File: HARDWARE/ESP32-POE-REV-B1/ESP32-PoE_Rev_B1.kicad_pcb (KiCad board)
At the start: 2 copper layers, 28 x 75 mm, 123 parts, among them Q1 Q12MHz/20pF/10ppm/4P/3.2x2.5mm, Q2 BC817-40(SOT23), Q3 BC817-40(SOT23), T1 DTC114YKA(SOT-23), U1 CH340T(SSOP20W), U3 MCP73833(MSOP10), U4 LAN8710A-EZC(QFN32), U7 SY8089AAAC(SOT23-5), U8 Si3402-B-GM(QFN-20_5x5mm), U9 ESP-WROOM-32

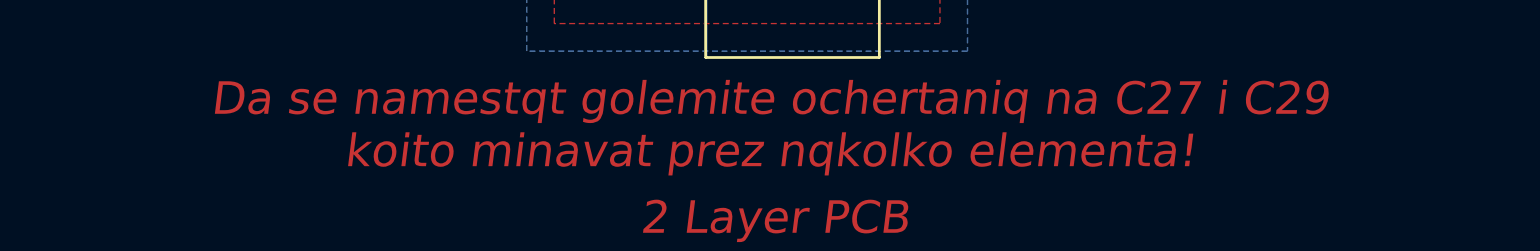
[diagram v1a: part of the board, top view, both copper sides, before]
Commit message: Update
Removed redundant text
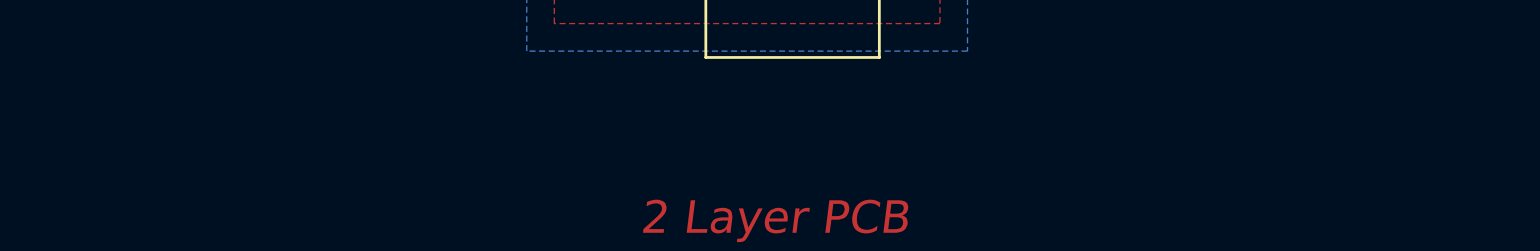
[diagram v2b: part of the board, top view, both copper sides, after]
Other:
- board text removed: "Da se namestqt golemite ochertaniq na C27 i C29 koito minavat prez nqkolko elementa!"
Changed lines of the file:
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@@
-(kicad_pcb (version 20171130) (host pcbnew 6.0.0-rc1-unknown-f85b147~66~ubuntu16.04.1)
+(kicad_pcb (version 20171130) (host pcbnew 6.0.0-rc1-unknown-80b25aa~66~ubuntu16.04.1)
   (general
     (thickness 1.6)
-    (drawings 24)
+    (drawings 23)
     (tracks 2605)
     (zones 0)
@@
     (35 F.Paste user hide)
     (36 B.SilkS user)
-    (37 F.SilkS user hide)
+    (37 F.SilkS user)
     (38 B.Mask user hide)
     (39 F.Mask user hide)
@@
     (effects (font (size 1.016 1.016) (thickness 0.254)))
   )
-  (gr_text "Da se namestqt golemite ochertaniq na C27 i C29 \nkoito minavat prez nqkolko elementa!" (at 106.2482 182.0672) (layer F.Cu)
-    (effects (font (size 3 3) (thickness 0.5) italic))
-  )
   (gr_text 1 (at 108.839 108.585) (layer B.SilkS)
     (effects (font (size 0.762 0.762) (thickness 0.1905)) (justify mirror))
@@
   (segment (start 111.125 127.762) (end 112.014 127.762) (width 0.4064) (layer B.Cu) (net 45))
   (segment (start 110.998 127.635) (end 111.125 127.762) (width 0.4064) (layer B.Cu) (net 45))
-  (segment (start 92.326 159.742) (end 92.326 156.742) (width 1.016) (layer F.Cu) (net 132))
-  (segment (start 92.326 159.742) (end 92.326 161.16) (width 1.016) (layer F.Cu) (net 132))
-  (segment (start 93.008 161.842) (end 93.476 161.842) (width 1.016) (layer F.Cu) (net 132))
-  (segment (start 92.326 161.16) (end 93.008 161.842) (width 1.016) (layer F.Cu) (net 132))
-  (segment (start 93.008 154.642) (end 93.476 154.642) (width 1.016) (layer F.Cu) (net 132))
-  (segment (start 92.326 155.324) (end 93.008 154.642) (width 1.016) (layer F.Cu) (net 132))
-  (segment (start 92.326 156.742) (end 92.326 155.324) (width 1.016) (layer F.Cu) (net 132))
   (segment (start 109.44 116.078) (end 110.202 115.316) (width 0.508) (layer B.Cu) (net 45))
   (segment (start 110.202 115.316) (end 111.125 115.316) (width 0.508) (layer B.Cu) (net 45))
@@
   (segment (start 95.24746 123.82246) (end 95.24746 123.53036) (width 0.4064) (layer B.Cu) (net 131))
   (segment (start 95.758 124.333) (end 95.24746 123.82246) (width 0.4064) (layer B.Cu) (net 131))
+  (segment (start 92.326 159.742) (end 92.326 156.742) (width 1.016) (layer F.Cu) (net 132))
+  (segment (start 92.326 159.742) (end 92.326 161.16) (width 1.016) (layer F.Cu) (net 132))
+  (segment (start 93.008 161.842) (end 93.476 161.842) (width 1.016) (layer F.Cu) (net 132))
+  (segment (start 92.326 161.16) (end 93.008 161.842) (width 1.016) (layer F.Cu) (net 132))
+  (segment (start 93.008 154.642) (end 93.476 154.642) (width 1.016) (layer F.Cu) (net 132))
+  (segment (start 92.326 155.324) (end 93.008 154.642) (width 1.016) (layer F.Cu) (net 132))
+  (segment (start 92.326 156.742) (end 92.326 155.324) (width 1.016) (layer F.Cu) (net 132))
   (zone (net 2) (net_name GND) (layer B.Cu) (hatch edge 0.508)
     (priority 1)
